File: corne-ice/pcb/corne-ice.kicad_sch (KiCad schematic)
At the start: 90 parts, among them J2 OLED, J4 OLED, SW1 SW_PUSH, SW10 SW_PUSH, SW11 SW_PUSH, SW12 SW_PUSH, SW13 SW_PUSH, SW14 SW_PUSH, SW15 SW_PUSH, SW16 SW_PUSH, SW17 SW_PUSH, SW18 SW_PUSH, SW19 SW_PUSH, SW2 SW_PUSH, SW20 SW_PUSH, SW21 SW_PUSH, SW22 SW_PUSH, SW23 SW_PUSH, SW24 SW_PUSH, SW25 SW_PUSH, SW26 SW_PUSH, SW27 SW_PUSH, SW28 SW_PUSH, SW29 SW_PUSH, SW3 SW_PUSH, SW30 SW_PUSH, SW31 SW_PUSH, SW32 SW_PUSH, SW33 SW_PUSH, SW34 SW_PUSH, SW35 SW_PUSH, SW36 SW_PUSH, SW37 SW_PUSH, SW38 SW_PUSH, SW39 SW_PUSH, SW4 SW_PUSH, SW40 SW_PUSH, SW41 SW_PUSH, SW42 SW_PUSH, SW5 SW_PUSH, SW6 SW_PUSH, SW7 SW_PUSH, SW8 SW_PUSH, SW9 SW_PUSH, U1 ProMicro, U2 ProMicro

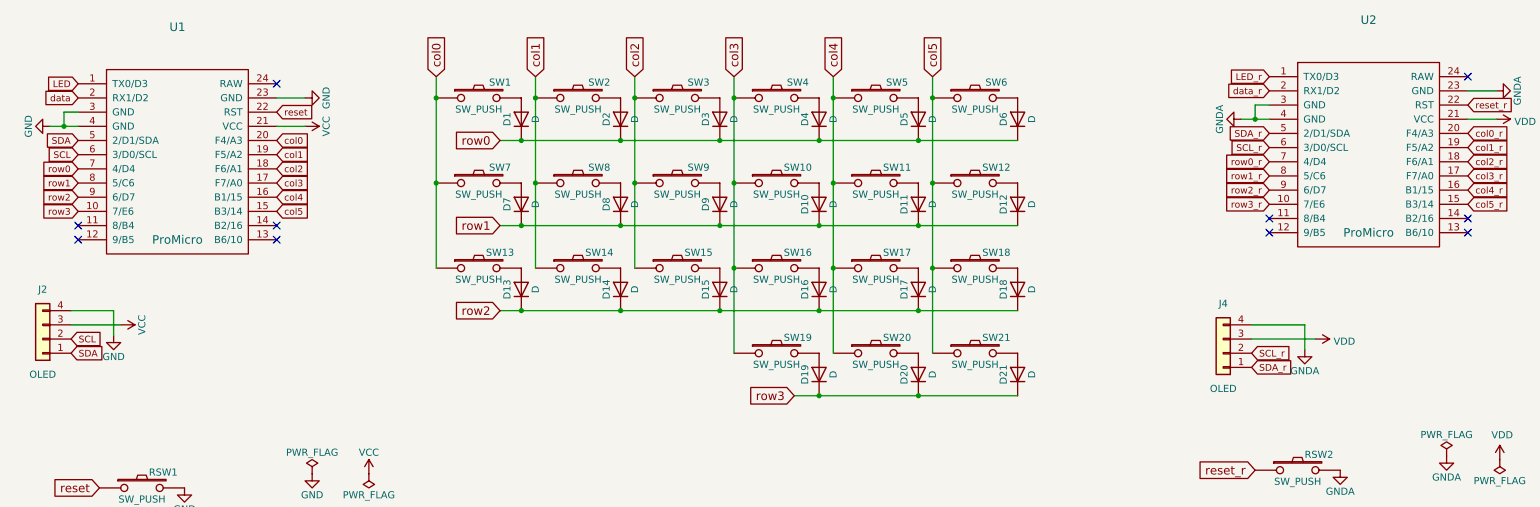
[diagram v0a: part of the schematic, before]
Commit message: update oled footprint and reroute
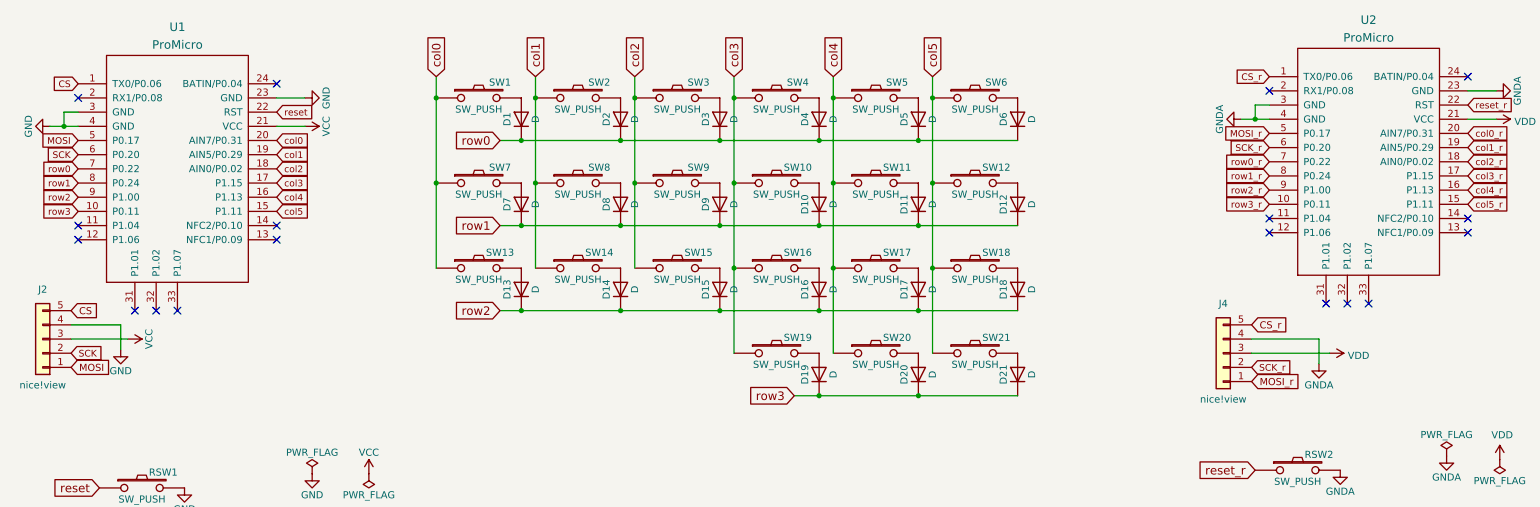
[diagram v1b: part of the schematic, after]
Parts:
- J2, J4: value OLED -> nice!view; footprint kbd:OLED_1side -> Connector_PinHeader_2.54mm:PinHeader_1x05_P2.54mm_Vertical; symbol Connector_Generic:Conn_01x04 -> Connector_Generic:Conn_01x05
- U1, U2: symbol kbd:ProMicro -> nice_nano:nice_nano
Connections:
- net LED renamed CS
- net CS: now also J2.5 (Pin_5)
- net LED_r renamed CS_r
- net CS_r: now also J4.5 (Pin_5)
- net SCL renamed SCK
- net SCL_r renamed SCK_r
- net SDA renamed MOSI
- net SDA_r renamed MOSI_r
- net data: no longer names the net of U1.2 (RX1/P0.08)
- net data_r: no longer names the net of U2.2 (RX1/P0.08)
- no-connect marks 10 -> 18

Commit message: place remaining footprints
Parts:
- added J1, J3: BAT, Connector_JST:JST_PH_S2B-PH-SM4-TB_1x02-1MP_P2.00mm_Horizontal, symbol Connector_Generic:Conn_01x02
- added PSW1, PSW2: SW_SPDT, keeblib:switch_SSSS811101, symbol Switch:SW_SPDT
- RSW1, RSW2: footprint kbd:ResetSW_1side -> keeblib:alps_sksn
- U1, U2: value ProMicro -> nice!nano
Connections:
- net GND: now also J1.2 (Pin_2)
- net GNDA: now also J3.2 (Pin_2)
- net RAW: now reaches U1.24 (BATIN/P0.04)
- net RAW: now also PSW1.1 (A)
- net RAW_r: now reaches U2.24 (BATIN/P0.04)
- net RAW_r: now also PSW2.1 (A)
- new net: J1.1 (Pin_1), PSW1.2 (B)
- new net: J3.1 (Pin_1), PSW2.2 (B)

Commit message: clean up, add gerber files
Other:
- company: foostan -> foostan/e3b0c442
- title: Corne Cherry -> Corne-ice
- moved on the sheet: D22, D23, D24, D25, D26, D27, D28, D29, D30, D31, D32, D33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
